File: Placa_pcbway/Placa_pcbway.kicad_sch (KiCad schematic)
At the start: 69 parts, among them J1 Screw_Terminal_Crusher1, J2 MixerScrewTerminal1, J3 FanScrewTerminal1, K1 FINDER-36.11, K2 FINDER-36.11, K3 FINDER-36.11, Q1 2N3904, Q2 2N3904, Q3 2N3904, U1 LM7805_TO220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

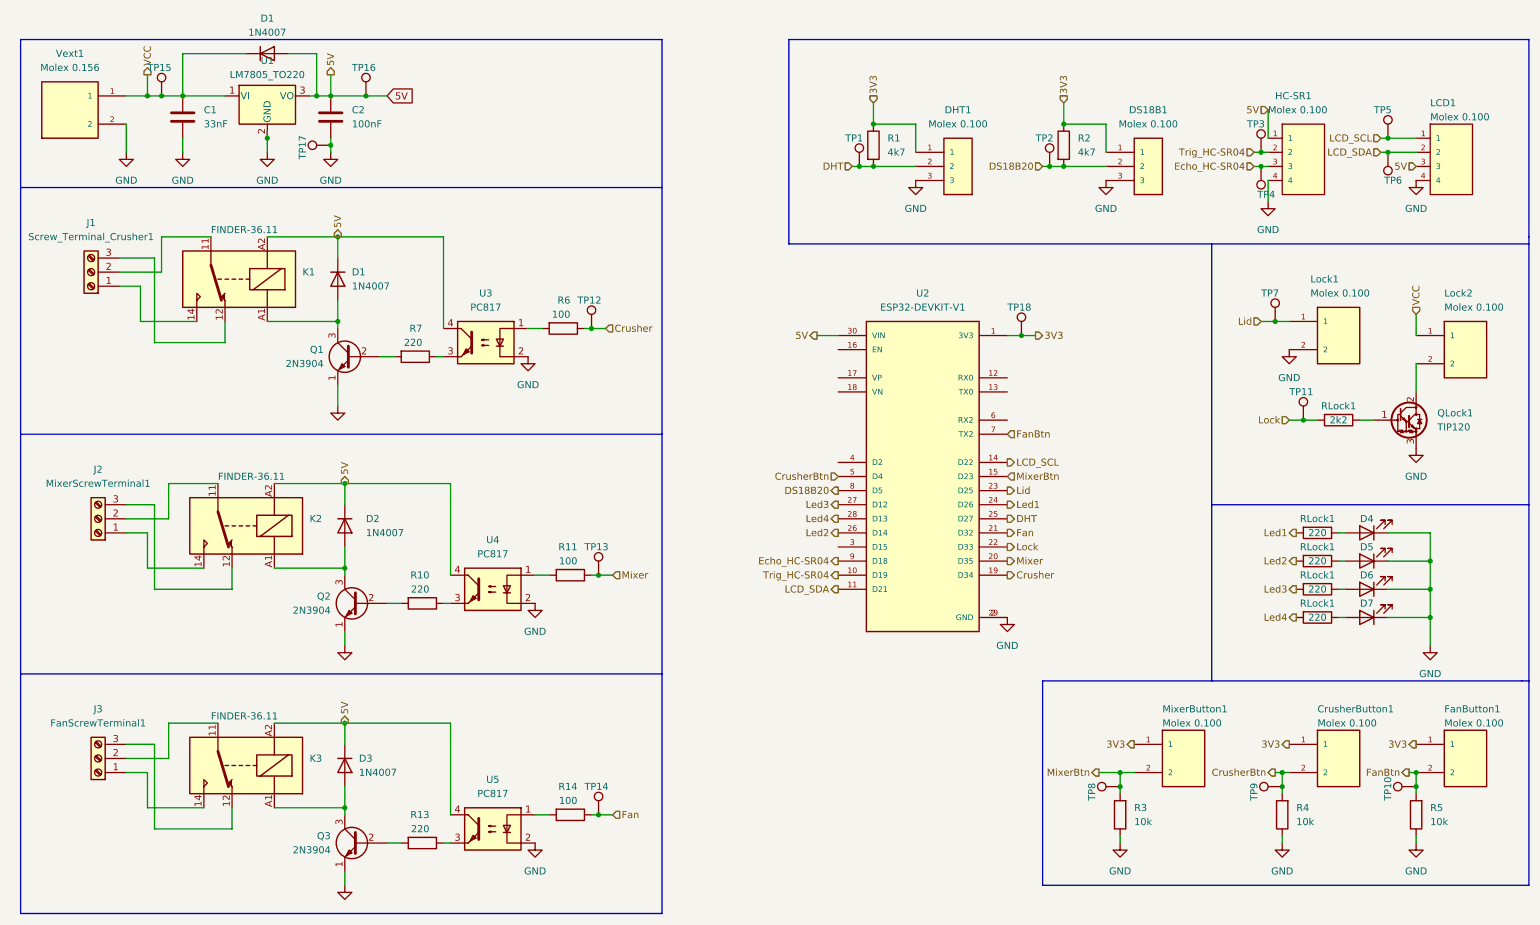
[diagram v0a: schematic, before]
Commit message: Placa pcbway terminada sin plano de tierra
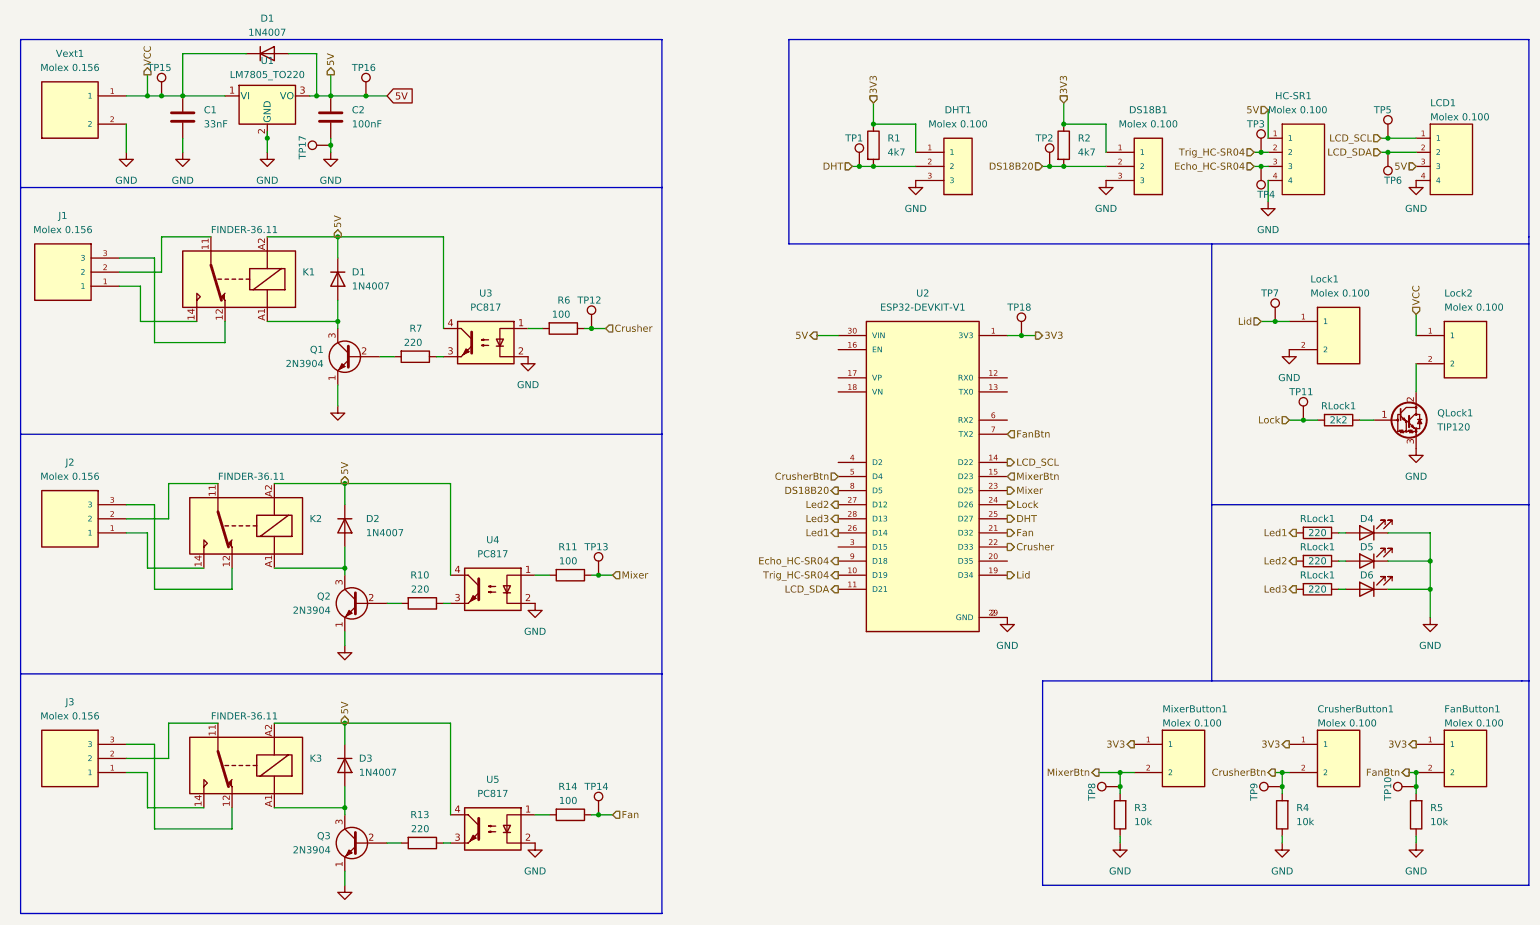
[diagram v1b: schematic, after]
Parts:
- removed D7: LED, LED_THT:LED_D5.0mm, symbol Device:LED
- removed J1: Screw_Terminal_Crusher1, TerminalBlock_4Ucon:TerminalBlock_4Ucon_1x03_P3.50mm_Vertical, symbol Connector:Screw_Terminal_01x03
- removed J2: MixerScrewTerminal1, TerminalBlock_4Ucon:TerminalBlock_4Ucon_1x03_P3.50mm_Vertical, symbol Connector:Screw_Terminal_01x03
- removed J3: FanScrewTerminal1, TerminalBlock_4Ucon:TerminalBlock_4Ucon_1x03_P3.50mm_Vertical, symbol Connector:Screw_Terminal_01x03
- removed RLock1: 220, Resistor_THT:R_Axial_DIN0309_L9.0mm_D3.2mm_P12.70mm_Horizontal, symbol Device:R
- added J1, J2, J3: Molex 0.156, Conectores_Molex:Molex_156_3pines, symbol Conectores_Molex:Molex_156_3pines
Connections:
- net Led4 is gone; now on net Led3: U2.28 (D13)
- net Crusher: now also U2.22 (D33); no longer U2.19 (D34)
- net Led1: now also U2.26 (D14); no longer U2.24 (D26)
- net Led2: now also U2.27 (D12); no longer U2.26 (D14)
- net Led3: no longer U2.27 (D12)
- net Lid: now also U2.19 (D34); no longer U2.23 (D25)
- net Lock: now also U2.24 (D26); no longer U2.22 (D33)
- net Mixer: now also U2.23 (D25); no longer U2.20 (D35)
- net at K2.14: now also J2.1
- net at K2.11: now also J2.2
- net at K2.12: now also J2.3
- net at K1.11: now also J1.2
- net at K1.12: now also J1.3
- net at K1.14: now also J1.1
- net at K3.11: now also J3.2
- net at K3.12: now also J3.3
- net at K3.14: now also J3.1

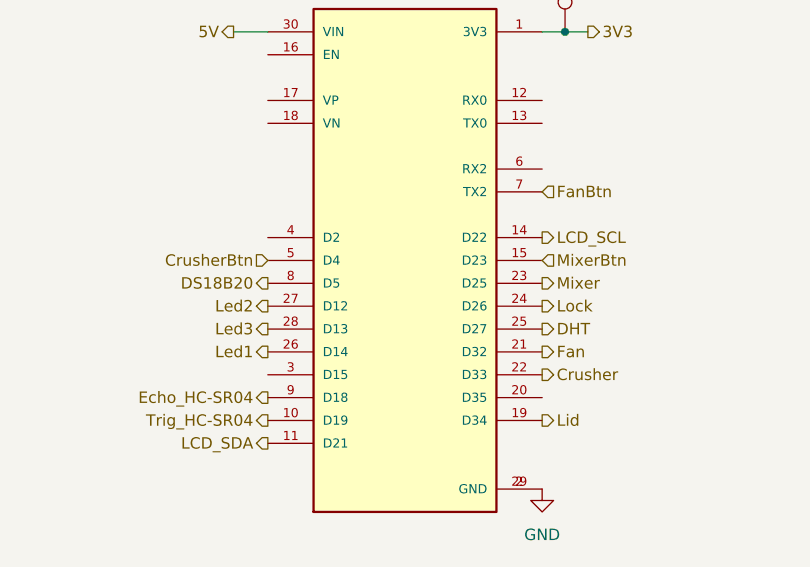
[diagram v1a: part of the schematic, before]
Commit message: Cambio de pin Fan Button
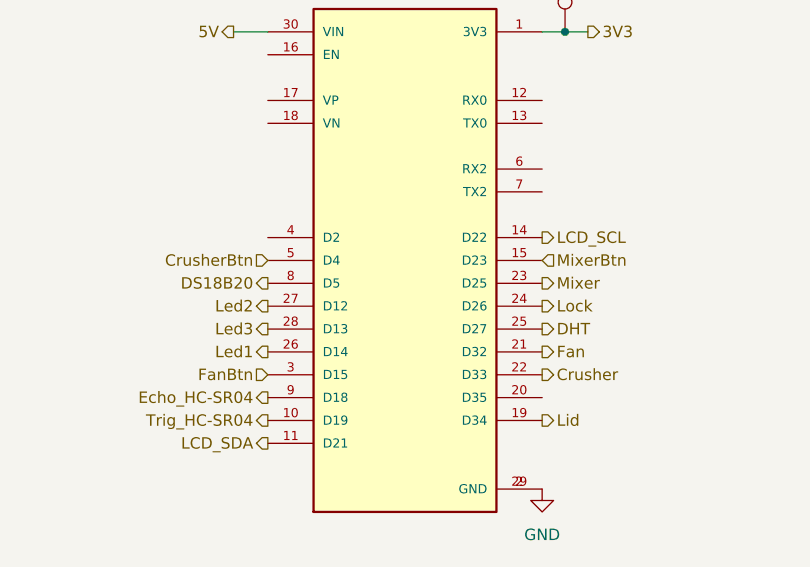
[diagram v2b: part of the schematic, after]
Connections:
- net FanBtn: now also U2.3 (D15); no longer U2.7 (TX2)
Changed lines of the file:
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@@
     (effects (font (size 1.27 1.27)) (justify left))
   )
-  (hierarchical_label "FanBtn" (shape input) (at 190.5 83.82 0) (fields_autoplaced)
-    (effects (font (size 1.27 1.27)) (justify left))
+  (hierarchical_label "FanBtn" (shape input) (at 160.02 104.14 180) (fields_autoplaced)
+    (effects (font (size 1.27 1.27)) (justify right))
   )
   (hierarchical_label "Crusher" (shape input) (at 118.11 64.77 0) (fields_autoplaced)

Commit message: Placa terminada sin plano
Placa terminada:
- Disñeos 3D agregados
- TP y Molex alineados
- Conexiones terminadas
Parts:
- removed LCD1: Molex 0.100, Conectores_Molex:Molex_100_4pines, symbol Conectores_Molex:Molex_100_4pines
- added HC-SR1: Molex 0.100, Conectores_Molex:Molex_100_4pines, symbol Conectores_Molex:Molex_100_4pines
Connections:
- net 5V: now also HC-SR1.4, HC-SR1.2; no longer HC-SR1.1
- net Echo_HC-SR04: now also HC-SR1.2; no longer HC-SR1.3
- net GND: now also HC-SR1.1, HC-SR1.1; no longer HC-SR1.4
- net LCD_SCL: now also HC-SR1.4
- net LCD_SDA: now also HC-SR1.3
- net Trig_HC-SR04: now also HC-SR1.3; no longer HC-SR1.2
